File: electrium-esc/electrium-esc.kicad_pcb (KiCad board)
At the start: 2 copper layers, 187 parts, among them J1 Conn_01x04_Male, J2 USB_MICRO, J3 Conn_01x03_Male, J4 Conn_01x04_Male, J5 Debug Connector, Q1 IRFS7530TRLPBF, Q10 IRFS7530TRLPBF, Q11 IRFS7530TRLPBF, Q12 IRFS7530TRLPBF, Q2 IRFS7530TRLPBF, Q3 IRFS7530TRLPBF, Q4 IRFS7530TRLPBF, Q5 IRFS7530TRLPBF, Q6 IRFS7530TRLPBF, Q7 IRFS7530TRLPBF, Q8 IRFS7530TRLPBF, Q9 IRFS7530TRLPBF, SW1 SW_SPDT, U1 STM32F407ZGT6, U2 DRV8301DCAR, U3 SN65HVD232, U4 DRV8301DCAR, U5 NRF24L01_Breakout, Y1 25MHz

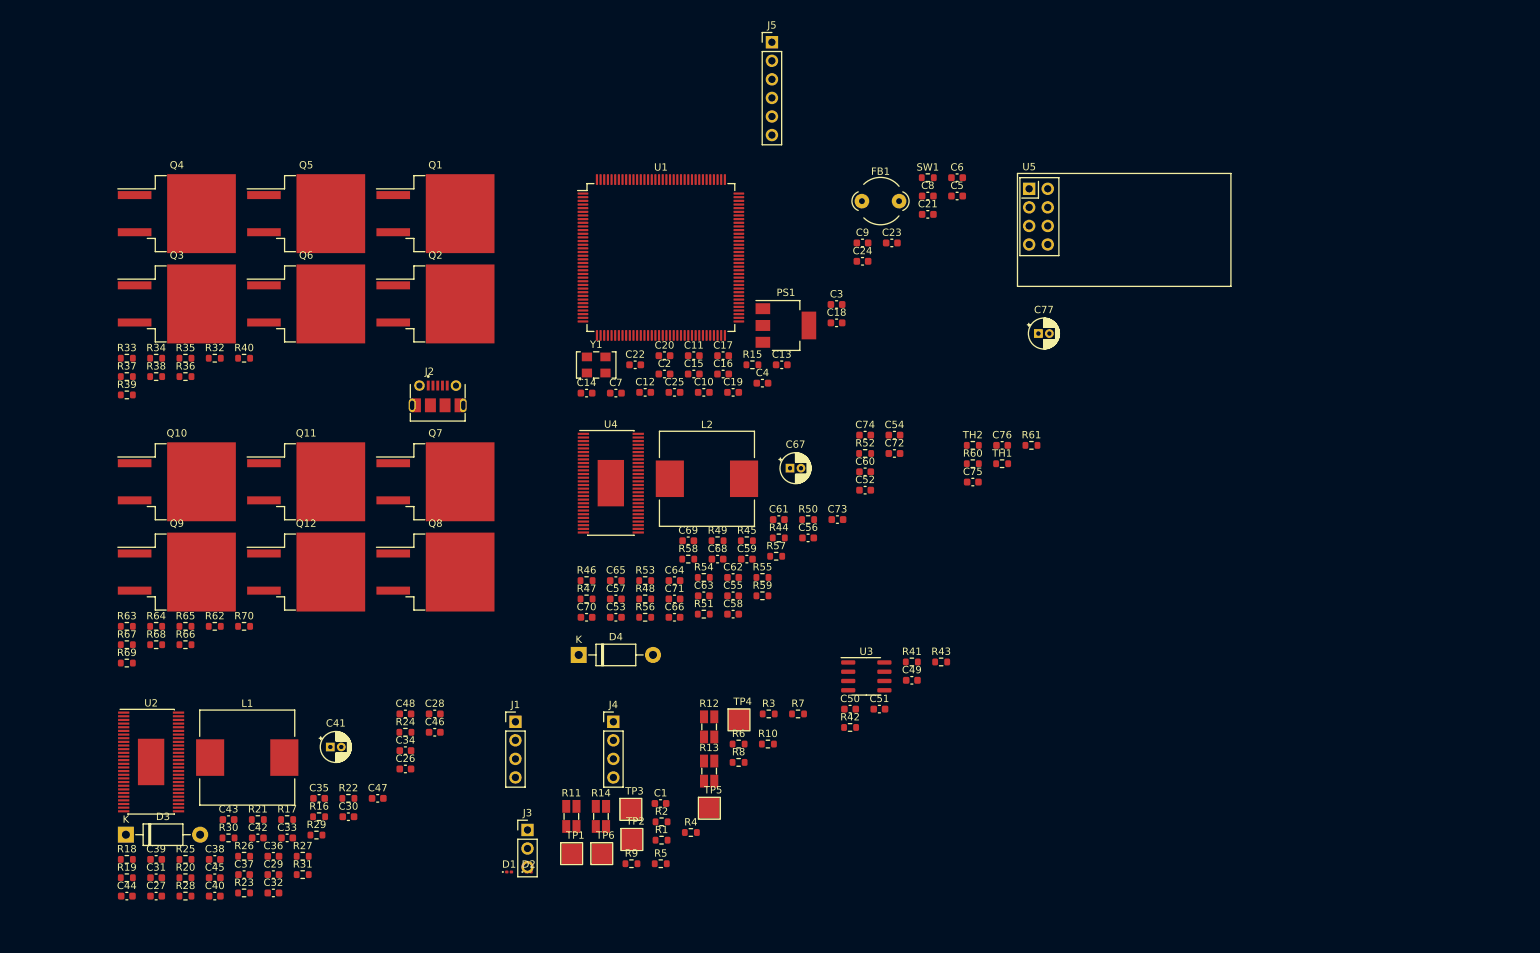
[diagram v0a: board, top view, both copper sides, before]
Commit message: initial pcb placement
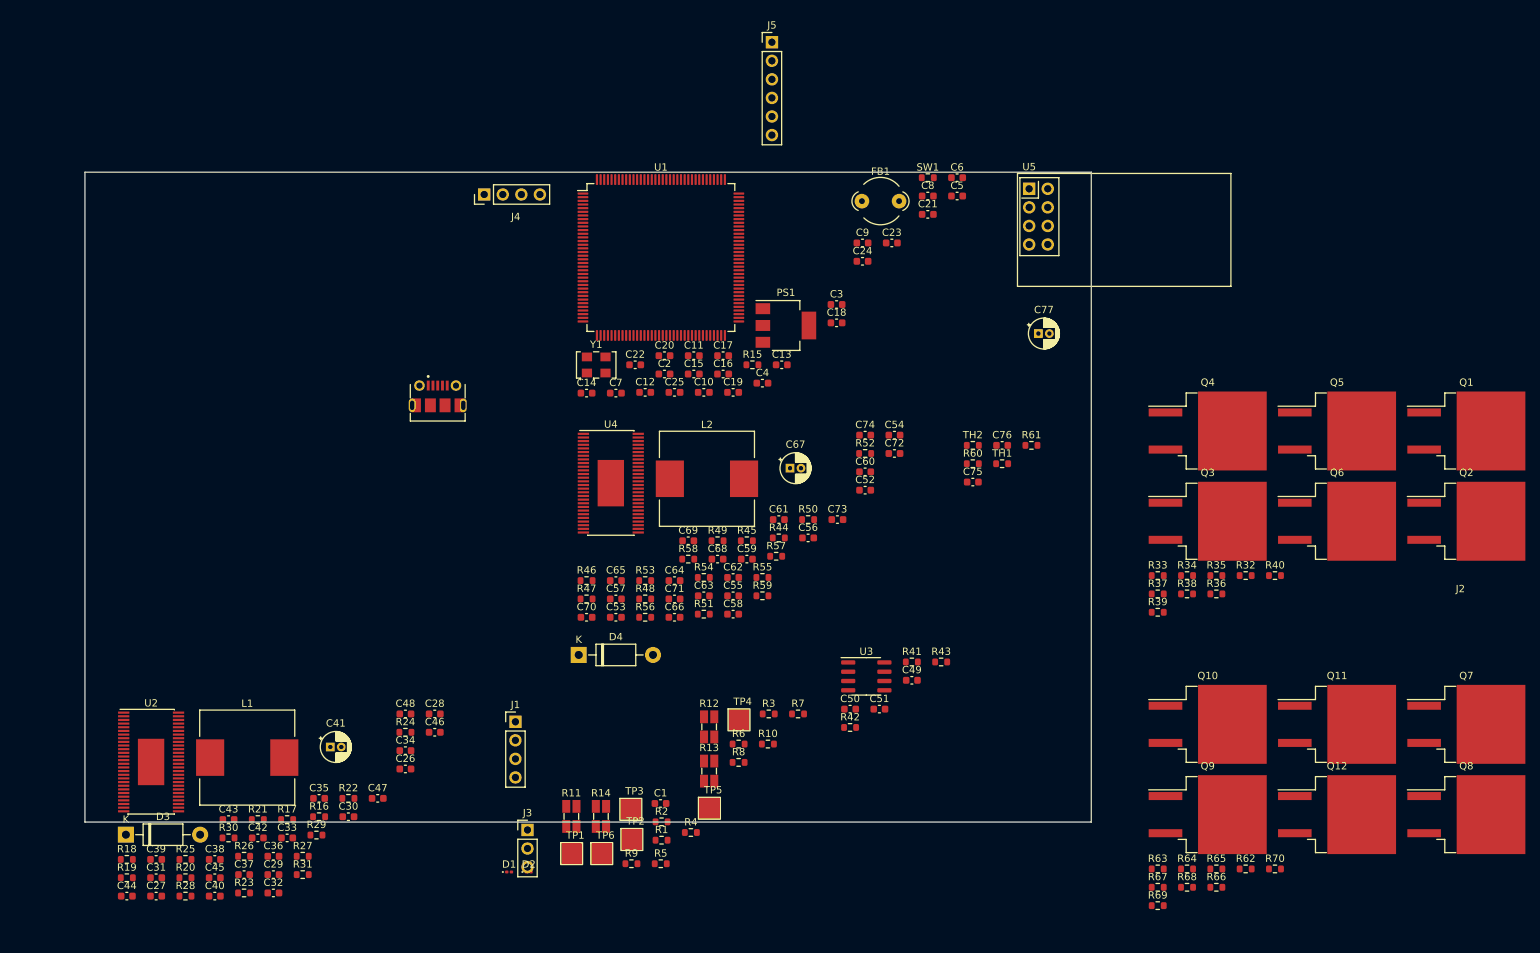
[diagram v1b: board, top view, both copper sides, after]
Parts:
- J4: value Conn_01x04_Male -> SERVO
- moved Q10 144.9 mm to (224.7, 111.1)
- moved Q11 144.9 mm to (242.4, 111.1)
- moved Q12 144.9 mm to (242.4, 123.4)
- moved Q7 144.9 mm to (260.1, 111.1)
- moved Q8 144.9 mm to (260.1, 123.4)
- moved Q9 144.9 mm to (224.7, 123.4)
- moved R62 144.9 mm to (229.9, 130.9)
- moved R63 144.9 mm to (217.9, 130.9)
- moved R64 144.9 mm to (221.9, 130.9)
- moved R67 144.9 mm to (217.9, 133.4)
- moved R68 144.9 mm to (221.9, 133.4)
- moved R69 144.9 mm to (217.9, 135.9)
- moved R70 144.9 mm to (233.9, 130.9)
- moved R65 144.9 mm to (225.9, 130.9)
- moved R66 144.9 mm to (225.9, 133.4)
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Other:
- board outline added: 137.7 x 88.9 mm

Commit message: Finished basic layout
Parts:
- removed D3, D4: 1N5819, Diode_THT:D_DO-41_SOD81_P10.16mm_Horizontal
- added R57: 1k5, Resistor_SMD:R_0603_1608Metric, F.Cu at (129.9, 23.5)
- C25: renamed from C42; moved to B.Cu
- C26: renamed from C44; moved to B.Cu
- C27: renamed from C45; moved to B.Cu
- C28: renamed from C46; moved to B.Cu
- C29: renamed from C47; moved to B.Cu
- C30: renamed from C48; moved to B.Cu
- C36: renamed from C34; moved to B.Cu
- C38: renamed from C35; moved to B.Cu
- C40: renamed from C36; moved to B.Cu
- C42: renamed from C43; moved to B.Cu
- C44: renamed from C31; moved to B.Cu
- C55: renamed from C52; moved to B.Cu
- C59: renamed from C60; moved to B.Cu
- C60: renamed from C53; moved to B.Cu
- C61: moved to B.Cu
- C63: renamed from C62; moved to B.Cu
- C66: renamed from C54; moved to B.Cu
- C67: renamed from C57; moved to B.Cu
- J4: renamed from J3; value Conn_01x03_Male -> SERVO
- J5: renamed from J4; value SERVO -> Conn_01x04_Male
- L1, L2: footprint Inductor_SMD:L_Wuerth_HCI-1335 -> Inductor_SMD:L_Vishay_IHLP-2020
- Q1, Q10, Q11, Q12, Q2, Q3, Q4, Q5, Q6, Q7, Q8, Q9: value IRFS7530TRLPBF -> IRF3205; footprint Package_TO_SOT_SMD:TO-263-2 -> Package_TO_SOT_THT:TO-220-3_Vertical
- R10: renamed from R24; moved to B.Cu
- R11: renamed from R29; moved to B.Cu
- R12: renamed from R27; moved to B.Cu
- R13: renamed from R30; moved to B.Cu
- R15: renamed from R28; moved to B.Cu
- R16: renamed from R25; moved to B.Cu
- R17: renamed from R31; moved to B.Cu
- R19: renamed from R44; moved to B.Cu
- R21: renamed from R45; moved to B.Cu
- R23: renamed from R48; moved to B.Cu
- R34: renamed from R32; footprint Resistor_SMD:R_0603_1608Metric -> Resistor_SMD:R_0805_2012Metric
- R35: footprint Resistor_SMD:R_0603_1608Metric -> Resistor_SMD:R_0805_2012Metric
- R36: renamed from R38; footprint Resistor_SMD:R_0603_1608Metric -> Resistor_SMD:R_0805_2012Metric
- R37: renamed from R33; footprint Resistor_SMD:R_0603_1608Metric -> Resistor_SMD:R_0805_2012Metric; moved to B.Cu
- R38: renamed from R36; footprint Resistor_SMD:R_0603_1608Metric -> Resistor_SMD:R_0805_2012Metric; moved to B.Cu
- R39: footprint Resistor_SMD:R_0603_1608Metric -> Resistor_SMD:R_0805_2012Metric; moved to B.Cu
- R40: renamed from R34; footprint Resistor_SMD:R_0603_1608Metric -> Resistor_SMD:R_0805_2012Metric; moved to B.Cu
- R41: renamed from R37; footprint Resistor_SMD:R_0603_1608Metric -> Resistor_SMD:R_0805_2012Metric; moved to B.Cu
- R42: renamed from R40; footprint Resistor_SMD:R_0603_1608Metric -> Resistor_SMD:R_0805_2012Metric; moved to B.Cu
- R43: renamed from R62; footprint Resistor_SMD:R_0603_1608Metric -> Resistor_SMD:R_0805_2012Metric
- R44: renamed from R65; footprint Resistor_SMD:R_0603_1608Metric -> Resistor_SMD:R_0805_2012Metric
- R45: renamed from R68; footprint Resistor_SMD:R_0603_1608Metric -> Resistor_SMD:R_0805_2012Metric
- R46: renamed from R63; footprint Resistor_SMD:R_0603_1608Metric -> Resistor_SMD:R_0805_2012Metric; moved to B.Cu
- R47: renamed from R66; footprint Resistor_SMD:R_0603_1608Metric -> Resistor_SMD:R_0805_2012Metric; moved to B.Cu
- R48: renamed from R69; footprint Resistor_SMD:R_0603_1608Metric -> Resistor_SMD:R_0805_2012Metric; moved to B.Cu
- R49: renamed from R64; footprint Resistor_SMD:R_0603_1608Metric -> Resistor_SMD:R_0805_2012Metric; moved to B.Cu
- R50: renamed from R67; footprint Resistor_SMD:R_0603_1608Metric -> Resistor_SMD:R_0805_2012Metric; moved to B.Cu
- R51: renamed from R70; footprint Resistor_SMD:R_0603_1608Metric -> Resistor_SMD:R_0805_2012Metric; moved to B.Cu
- R55: renamed from R5; value 0 -> 22
- R56: renamed from R6; value 0 -> 22
- R65: renamed from R1; value 2k2 -> 220
- R8: renamed from R26; moved to B.Cu
- SW1: footprint Resistor_SMD:R_0603_1608Metric -> Button_Switch_THT:SW_CuK_JS202011CQN_DPDT_Straight
- moved C33 162.8 mm to (235.7, 53.4)
- moved R5 162.8 mm to (241.6, 45.9)
- moved R6 162.8 mm to (219.7, 53.9)
- moved R7 162.8 mm to (227.7, 53.9)
- moved C75 117.3 mm to (88.3, 88.0)
- moved C47 111.4 mm to (157.3, 48.5), turned to 180 degrees
- moved C46 104.7 mm to (157.3, 50.3), turned to 180 degrees
- moved C45 101.9 mm to (157.3, 52.1), turned to 180 degrees
- moved Q8 99.1 mm to (166.4, 91.2)
- moved Q7 98.5 mm to (166.2, 81.3)
- moved U5 97.1 mm to (107.4, 66.1), turned to 180 degrees
- moved Q2 96.1 mm to (166.5, 61.4)
- moved J5 95.9 mm to (62.9, 111.0)
- moved Q1 95.5 mm to (166.6, 51.5)
- moved R2 93.3 mm to (140.1, 61.0), turned to 180 degrees
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- renumbered C12 to C1, C11 to C10, C13 to C11, C16 to C12, C19 to C13, C22 to C14, C25 to C15, C14 to C16, C20 to C18, C23 to C19, C15 to C2, C2 to C20, C6 to C21, C8 to C22, C4 to C23, C5 to C24, C18 to C3, C29 to C31, C26 to C32, C37 to C33, C33 to C34, C41 to C35, C27 to C37, C30 to C39, C21 to C4, C40 to C41, C28 to C43, C32 to C45, C38 to C46, C39 to C47, C68 to C48, C70 to C49, C24 to C5, C71 to C50, C72 to C51, C73 to C52, C74 to C53, C55 to C54, C63 to C56, C59 to C57, C67 to C58, C3 to C6, C56 to C62, C66 to C64, C69 to C65, C58 to C68, C64 to C69, C65 to C70, C50 to C72, C51 to C73, C49 to C74, C77 to C75, C75 to C76, C76 to C77, C1 to C79, C9 to C8, C10 to C9, D1 to D5, D2 to D6, J5 to J1, J1 to J3, R15 to R1, R23 to R14, R46 to R18, R18 to R2, R49 to R20, R47 to R22, R54 to R24, R50 to R25, R52 to R26, R57 to R27, R55 to R28, R58 to R29, R16 to R3, R51 to R30, R56 to R31, R53 to R32, R59 to R33, R21 to R4, R17 to R5, R2 to R52, R3 to R53, R4 to R54, R11 to R58, R13 to R59, R19 to R6, R12 to R60, R14 to R61, R7 to R62, R9 to R63, R10 to R64, R8 to R66, R41 to R68, R42 to R69, R20 to R7, R43 to R70, R60 to R71, R61 to R72, R22 to R9, U4 to U3, U3 to U4
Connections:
- net /CANH renamed /CAN+
- net /CANL renamed /CAN-
- net Net-(J2-Pad2) renamed /USB_D-
- net Net-(J2-Pad3) renamed /USB_D+
- Q10 pad 2: /Motor Driver B (DRV8301)/H2_VS -> /Motor Driver B (DRV8301)/H1_VS
- Q10 pad 3: GND -> /Motor Driver B (DRV8301)/H1_LOW
- Q11 pad 2: V_SUPPLY -> /Motor Driver B (DRV8301)/H2_VS
- Q11 pad 3: /Motor Driver B (DRV8301)/H3_VS -> GND
- Q2 pad 2: /Motor Driver A (DRV8301)/H1_VS -> V_SUPPLY
- Q2 pad 3: /Motor Driver A (DRV8301)/H1_LOW -> /Motor Driver A (DRV8301)/H2_VS
- Q3 pad 3: /Motor Driver A (DRV8301)/H2_VS -> /Motor Driver A (DRV8301)/H3_VS
- Q4 pad 2: /Motor Driver A (DRV8301)/H2_VS -> /Motor Driver A (DRV8301)/H1_VS
- Q4 pad 3: GND -> /Motor Driver A (DRV8301)/H1_LOW
- Q5 pad 2: V_SUPPLY -> /Motor Driver A (DRV8301)/H2_VS
- Q5 pad 3: /Motor Driver A (DRV8301)/H3_VS -> GND
- Q8 pad 2: /Motor Driver B (DRV8301)/H1_VS -> V_SUPPLY
- Q8 pad 3: /Motor Driver B (DRV8301)/H1_LOW -> /Motor Driver B (DRV8301)/H2_VS
- Q9 pad 3: /Motor Driver B (DRV8301)/H2_VS -> /Motor Driver B (DRV8301)/H3_VS
- R35 pad 1: Net-(Q3-Pad1) -> Net-(Q2-Pad1)
- R36 pad 1: Net-(Q5-Pad1) -> Net-(Q3-Pad1)
- R37 pad 2: Net-(Q2-Pad1) -> Net-(Q4-Pad1)
- R38 pad 1: Net-(Q4-Pad1) -> Net-(Q5-Pad1)
- R40 pad 1: Net-(Q2-Pad1) -> Net-(Q4-Pad1)
- R41 pad 2: Net-(Q4-Pad1) -> Net-(Q5-Pad1)
- R44 pad 1: Net-(Q9-Pad1) -> Net-(Q8-Pad1)
- R45 pad 1: Net-(Q11-Pad1) -> Net-(Q9-Pad1)
- R46 pad 2: Net-(Q8-Pad1) -> Net-(Q10-Pad1)
- R47 pad 1: Net-(Q10-Pad1) -> Net-(Q11-Pad1)
- R49 pad 1: Net-(Q8-Pad1) -> Net-(Q10-Pad1)
- R50 pad 2: Net-(Q10-Pad1) -> Net-(Q11-Pad1)
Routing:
- net +3.3V: track 0.00 -> 35.0 mm
- net GND: track 0.00 -> 5.19 mm
- added copper zone on F.Cu, net V_SUPPLY
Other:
- board size 137.7 x 88.9 mm -> 94.1 x 71.6 mm

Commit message: Semi-finished schematic
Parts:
- added D1: 1N5819, Diode_THT:D_DO-41_SOD81_P10.16mm_Horizontal, F.Cu at (185.5, 40.6)
- added D2: 1N5819, Diode_THT:D_DO-41_SOD81_P10.16mm_Horizontal, F.Cu at (204.0, 40.6)
- added D3: 1N5819, Diode_THT:D_DO-41_SOD81_P10.16mm_Horizontal, F.Cu at (185.5, 27.9)
- added D4: 1N5819, Diode_THT:D_DO-41_SOD81_P10.16mm_Horizontal, F.Cu at (185.5, 32.1)
- C11, C12, C13, C14, C15, C16, C20, C31, C32, C34, C37, C39, C43, C62, C65, C68, C69, C70, R2, R26, R34, R35, R43, R5, R71, R72, R9: moved to B.Cu
- C28, C29, C30, C66, C67: moved to F.Cu
- moved TP1 136.7 mm to (186.1, 51.6)
- moved C76 118.6 mm to (106.4, 102.9)
- moved C77 118.6 mm to (110.4, 97.8)
- moved R72 109.9 mm to (120.8, 83.2), turned to 90 degrees
- moved R71 103.4 mm to (119.0, 83.2), turned to 90 degrees
- moved R5 97.5 mm to (145.2, 60.1), turned to 90 degrees
- moved R55 94.9 mm to (139.7, 56.9), turned to 90 degrees
- moved R7 88.5 mm to (139.8, 64.3)
- moved TH2 81.4 mm to (140.8, 77.5), turned to -90 degrees
- moved R6 80.3 mm to (139.8, 62.7)
- moved C33 78.4 mm to (157.5, 58.8), turned to -90 degrees
- moved SW1 77.9 mm to (105.2, 62.0), turned to 90 degrees
- moved R56 74.2 mm to (137.2, 56.9), turned to 90 degrees
- moved C49 64.3 mm to (166.1, 74.7)
- moved C54 55.8 mm to (140.3, 80.8)
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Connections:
- U1 pad 46: /MCU (STM32F407ZGT6)/L3_B -> /MCU (STM32F407ZGT6)/H3_B
- U1 pad 47: /MCU (STM32F407ZGT6)/H3_B -> /MCU (STM32F407ZGT6)/L3_B
- U1 pad 73: unconnected-(U1-Pad73) -> /MCU (STM32F407ZGT6)/EN_GATE_B
- U1 pad 74: /MCU (STM32F407ZGT6)/CS_B -> /MCU (STM32F407ZGT6)/DC_CAL_B
- U1 pad 77: unconnected-(U1-Pad77) -> /MCU (STM32F407ZGT6)/CS_B
- U1 pad 87: /MCU (STM32F407ZGT6)/EN_GATE_B -> unconnected-(U1-Pad87)
- U1 pad 88: /MCU (STM32F407ZGT6)/DC_CAL_B -> unconnected-(U1-Pad88)
- U1 pad 90: /MCU (STM32F407ZGT6)/EN_GATE_A -> unconnected-(U1-Pad90)
- U1 pad 91: /MCU (STM32F407ZGT6)/DC_CAL_A -> unconnected-(U1-Pad91)
- U1 pad 98: unconnected-(U1-Pad98) -> /MCU (STM32F407ZGT6)/EN_GATE_A
- U1 pad 99: unconnected-(U1-Pad99) -> /MCU (STM32F407ZGT6)/DC_CAL_A
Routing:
- net /Motor Driver A (DRV8301)/H1_VS: track 0.00 -> 68.8 mm, vias 0 -> 3
- net /Motor Driver A (DRV8301)/H2_VS: track 0.00 -> 54.0 mm, vias 0 -> 2
- net +3.3V: track 35.0 -> 87.8 mm, vias 0 -> 10
- net V_SUPPLY: track 0.00 -> 50.9 mm, vias 0 -> 1
- net /Motor Driver B (DRV8301)/H1_LOW: track 0.00 -> 50.6 mm, vias 0 -> 2
- net /Motor Driver A (DRV8301)/H3_VS: track 0.00 -> 47.8 mm, vias 0 -> 2
- net /Motor Driver A (DRV8301)/H1_LOW: track 0.00 -> 47.7 mm, vias 0 -> 2
- net NRST: track 0.00 -> 35.1 mm, vias 0 -> 1
- net /Motor Driver B (DRV8301)/H3_LOW: track 0.00 -> 34.6 mm, vias 0 -> 1
- net Net-(Q5-Pad1): track 0.00 -> 28.8 mm
- net /Motor Driver A (DRV8301)/M_L1: track 0.00 -> 28.8 mm, vias 0 -> 1
- net Net-(Q4-Pad1): track 0.00 -> 27.3 mm
- net /Motor Driver A (DRV8301)/H3_LOW: track 0.00 -> 27.3 mm
- net /MCU (STM32F407ZGT6)/L3_B: track 0.00 -> 27.1 mm
- net /MCU (STM32F407ZGT6)/H3_B: track 0.00 -> 26.4 mm
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- added copper zone on F.Cu, net +3.3V
- added copper zone on F.Cu, net +5V
- added copper zone on F.Cu, net /Motor Driver A (DRV8301)/H1_VS
- added copper zone on F.Cu, net /Motor Driver A (DRV8301)/H2_VS
- added copper zone on F.Cu, net /Motor Driver A (DRV8301)/H3_VS
- added copper zone on F.Cu, net /Motor Driver B (DRV8301)/H1_VS
- added copper zone on F.Cu, net /Motor Driver B (DRV8301)/H2_VS
- added copper zone on F.Cu, net /Motor Driver B (DRV8301)/H3_VS
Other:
- board size 94.1 x 71.6 mm -> 87.1 x 57.9 mm

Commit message: Update more components and few traces
Final design hopefully done by tomorrow. Logistical problems are coming through, needs to suit components to those needs
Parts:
- removed FB1: 120R, Ferrite_THT:LairdTech_28C0236-0JW-10
- C10: value 10n -> 1u
- D1, D2, D3, D4: footprint Diode_THT:D_DO-41_SOD81_P10.16mm_Horizontal -> Diode_SMD:D_0603_1608Metric
- R24, R27, R28, R29, R31, R33, R55, R56: moved to B.Cu
- moved R33 73.1 mm to (120.9, 75.1), turned to -90 degrees
- moved D3 72.8 mm to (118.6, 56.5)
- moved R27 68.0 mm to (124.2, 75.1), turned to -90 degrees
- moved R28 67.7 mm to (122.6, 78.2), turned to -90 degrees
- moved D2 64.3 mm to (151.5, 77.7)
- moved R31 63.9 mm to (120.9, 78.2), turned to -90 degrees
- moved R24 61.7 mm to (124.2, 78.2), turned to -90 degrees
- moved C76 40.2 mm to (143.3, 118.8)
- moved C77 40.2 mm to (147.3, 113.8)
- moved C75 39.4 mm to (126.8, 96.5)
- moved D1 38.5 mm to (151.1, 57.9)
- moved R29 33.6 mm to (122.6, 75.1), turned to -90 degrees
- moved C6 13.7 mm to (129.2, 51.1), turned to 180 degrees
- moved U5 11.5 mm to (118.4, 101.6), turned to 180 degrees
- moved J4 9.94 mm to (81.5, 97.8)
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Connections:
- C10 pad 1: +3.3VA -> +3.3V
- C9 pad 1: +3.3VA -> +3.3V
- U1 pad 33: +3.3VA -> +3.3V
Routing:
- net +3.3V: track 87.8 -> 123.0 mm
- net /Motor Driver B (DRV8301)/H3_VS: track 25.8 -> 59.7 mm
- net SWDIO: track 0.00 -> 32.4 mm, vias 0 -> 1
- net /Motor Driver B (DRV8301)/H2_VS: track 20.4 -> 51.9 mm
- net /Motor Driver B (DRV8301)/H1_VS: track 22.0 -> 49.9 mm
- net SWCLK: track 0.00 -> 22.1 mm, vias 0 -> 1
- net /MCU (STM32F407ZGT6)/NRF_CSN: track 17.5 -> 0.00 mm
- net /MCU (STM32F407ZGT6)/USB_D-: track 15.4 -> 0.04 mm, vias 2 -> 0
- net /MCU (STM32F407ZGT6)/USB_D+: track 14.4 -> 0.00 mm, vias 2 -> 0
- net /MCU (STM32F407ZGT6)/SENS1_B: track 0.00 -> 13.4 mm, vias 0 -> 1
- net /MCU (STM32F407ZGT6)/SENS2_B: track 0.00 -> 12.1 mm, vias 0 -> 1
- net /MCU (STM32F407ZGT6)/NRF_MOSI: track 11.8 -> 0.00 mm
- net /MCU (STM32F407ZGT6)/NRF_CE: track 11.0 -> 0.00 mm, vias 1 -> 0
- net /MCU (STM32F407ZGT6)/SENS3_B: track 0.00 -> 10.6 mm, vias 0 -> 1
- net /Motor Driver B (DRV8301)/COMP: track 2.11 -> 10.8 mm, vias 0 -> 1
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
